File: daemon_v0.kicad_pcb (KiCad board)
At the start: 4 copper layers, 85.9 x 53.2 mm, 338 parts, among them J1 Battery PTC 2A Fuse, J10 USB-A♂ Charge Port 4, J11 USB-C♀ Main Port 5, J12 WAGO 4P Field Terminal, J13 USB-C♀ Goobay Bridge, J14 RJ45 MagJack, J15 TRRS 3.5mm Jack, J16 Speaker JST, J17 Analog-In, J2 10mΩ Current Sense, J3 40-Pin Radxa Header, J4 AUX GPIO Breakout, J6 ST7789 SPI Display, J7 USB-C♂ Plug → Radxa (KEY), J8 USB-A♀ Host Port 2, J9 USB-A♀ Host Port 3, K1 G6K-2F-Y, Q1 BC857 Dummy Load PNP, Q2 BSS84 Wake PMOS, Q3 2N7002 PMIC Kill NMOS, Q4 AO3400A IR Drive NMOS, Q5 AO3400A, SW1 Power Button, SW2 5-Way Nav Switch, U1 IP5328P PMIC, U10 MAX98357A I2S Amp, U11 ISO1212 Dual Isolator, U12 ESD USB Port1, U13 INMP441 Mic Left, U14 SL2.1A USB Hub 2, U15 SY6280 Port4 USB-A♂, U16 ESD USB Port2, U17 ESD USB Port3, U18 ESD USB Port4, U19 ESD USB Port5, U2 AP2112K 3.3V LDO, U20 ESD Goobay Bridge, U21 PCF8574 I2C GPIO Exp, U22 SY6280 Port5 USB-C♀, U23 3.3→5V Level Shifter, U24 INMP441 Mic Right, U25 ESD9B5.0ST5G, U26 ESD9B5.0ST5G, U27 NAU88C22, U28 ADS1115, U29 SP3485, U3 SL2.1A USB Hub 1, U30 TSOP38238, U31 ATECC608B, U32 74LVC04A, U33 TS3USB221, U34 TS3USB221, U35 TS3USB221, U36 TS3USB221, U37 TS3USB221, U4 SY6280 Port1 Radxa Key, U5 SY6280 Port2 USB-A♀, U6 SY6280 Port3 USB-A♀, U7 NE555 Heartbeat Timer, U8 CC1101 Sub-GHz Radio, U9 RTL8152B Ethernet, Y1 12MHz Hub1 Xtal, Y2 12MHz Hub2 Xtal, Y3 27MHz CC1101 Xtal, Y4 25MHz Ethernet Xtal

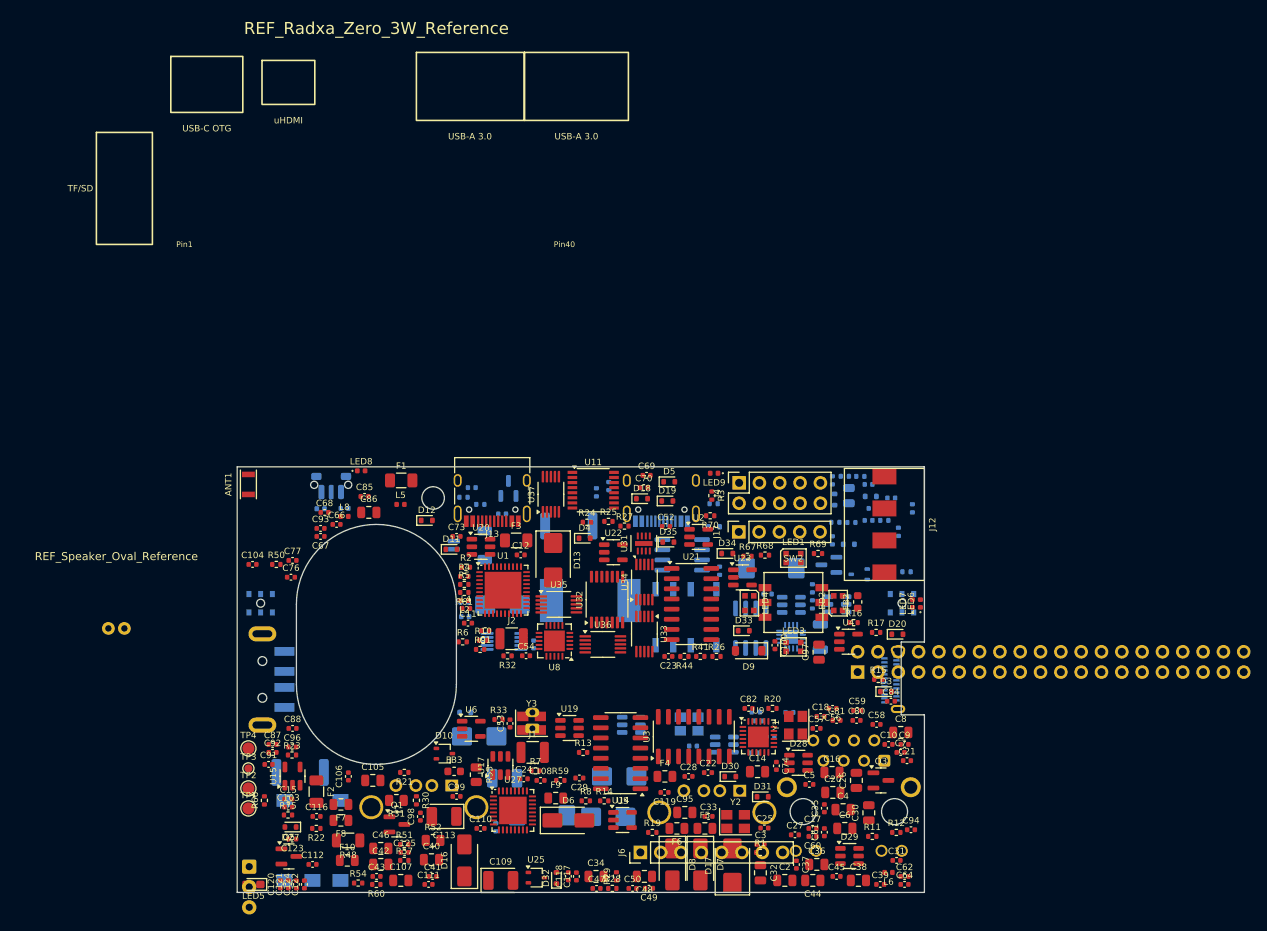
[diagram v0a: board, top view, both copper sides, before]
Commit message: fix: correct rotation on all 23 back-side components (flip negated rotation)
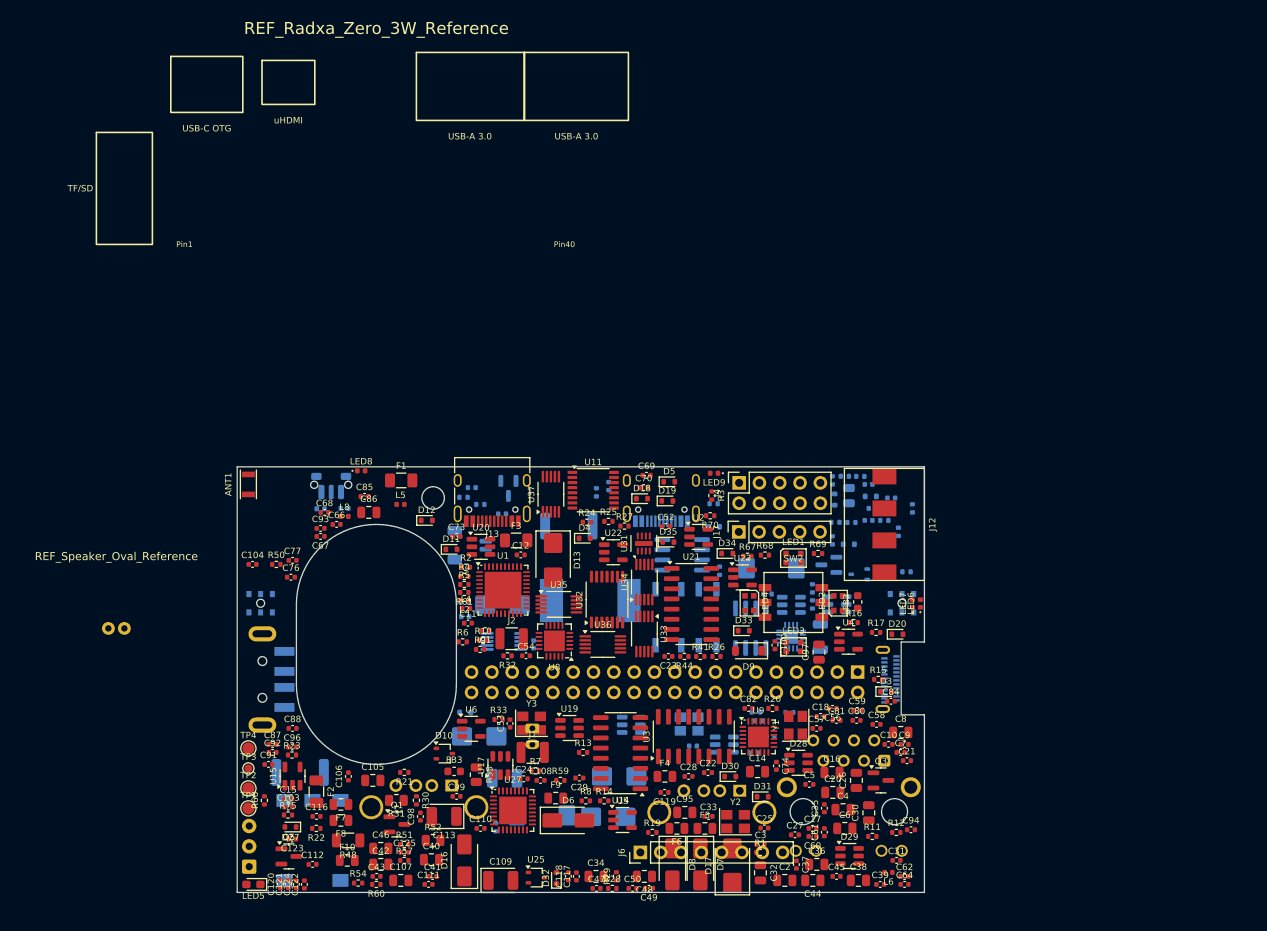
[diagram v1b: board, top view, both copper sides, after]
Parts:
- turned BAT1 to -90 degrees
- turned C55 to 90 degrees
- turned C71 to -90 degrees
- turned D24 to -90 degrees
- turned FB1 to 90 degrees
- turned J15 to 90 degrees
- turned J16 to 90 degrees
- turned J3 to 90 degrees
- turned J7 to -90 degrees
- turned K1 to -90 degrees
- turned Q2 to -90 degrees
- turned R18 to 90 degrees
- turned R34 to -90 degrees
- turned R36 to 90 degrees
- turned R38 to -90 degrees
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
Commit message: fix: restore board from screenshot4 (disk full corrupted file) + J6 rotated 180°
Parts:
- turned J6 to -90 degrees

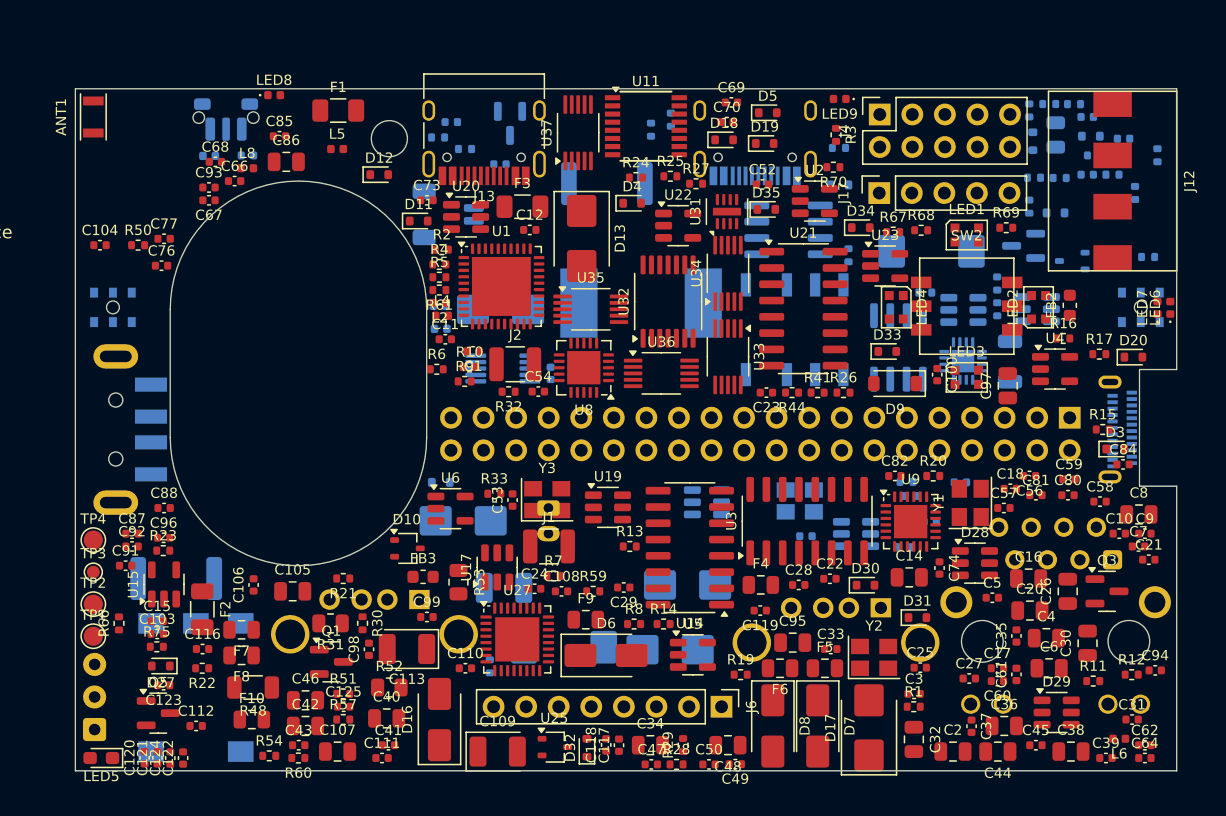
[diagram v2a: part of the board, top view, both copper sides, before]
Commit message: feat: Freerouting partial autoroute — ~100 nets routed, 406 need manual routing
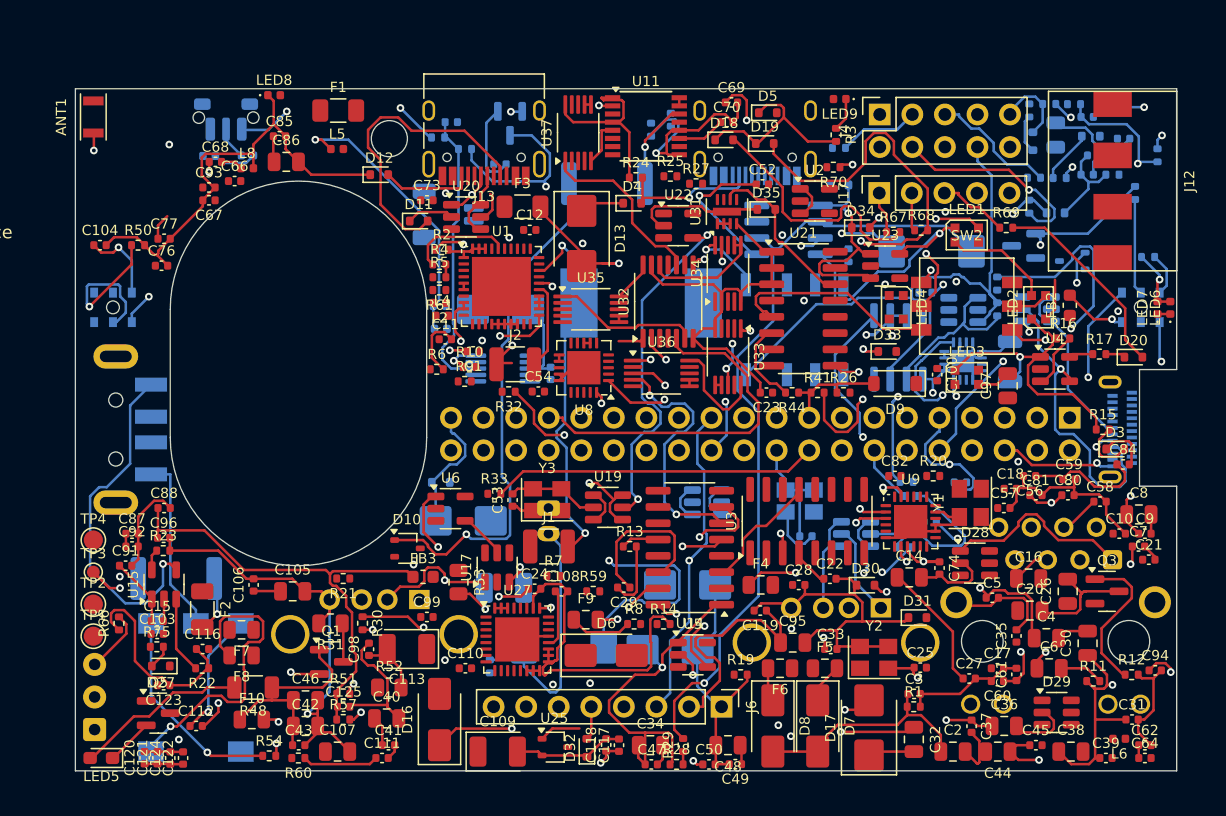
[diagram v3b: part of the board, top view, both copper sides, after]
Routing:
- net GND: track 0.00 -> 617.0 mm, vias 0 -> 9
- net 3V3_SYS: track 0.00 -> 211.7 mm, vias 0 -> 4
- net 5V_SYS: track 0.00 -> 200.7 mm, vias 0 -> 8
- net USB_VBUS_4: track 0.00 -> 121.8 mm, vias 0 -> 5
- net I2S_LRCLK: track 0.00 -> 105.2 mm, vias 0 -> 3
- net IR_RX: track 0.00 -> 102.6 mm, vias 0 -> 2
- net MIC_VDD: track 0.00 -> 99.0 mm, vias 0 -> 2
- net 5V_J4_OUT: track 0.00 -> 88.8 mm, vias 0 -> 2
- net IP5328P_VBUS: track 0.00 -> 76.6 mm, vias 0 -> 3
- net BAT: track 0.00 -> 68.9 mm, vias 0 -> 2
- net I2S_DATA_IN: track 0.00 -> 68.6 mm, vias 0 -> 2
- net BAT_ISO: track 0.00 -> 64.1 mm, vias 0 -> 4
- net NAV_CENTER: track 0.00 -> 64.0 mm, vias 0 -> 3
- net HB_TMR_THR: track 0.00 -> 62.5 mm, vias 0 -> 1
- net HB_TMR_OUT: track 0.00 -> 61.3 mm, vias 0 -> 3
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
